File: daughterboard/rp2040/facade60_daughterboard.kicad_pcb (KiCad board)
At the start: 2 copper layers, 29.2 x 43.8 mm, 38 parts, among them J1 Conn_01x30, J2 USB_C_Receptacle_USB2.0, SW1 BOOT, SW2 RESET, U1 SRV05-4, U2 RT9013-33GB, U3 W25Q128JVS, U4 RP2040, Y1 12MHz

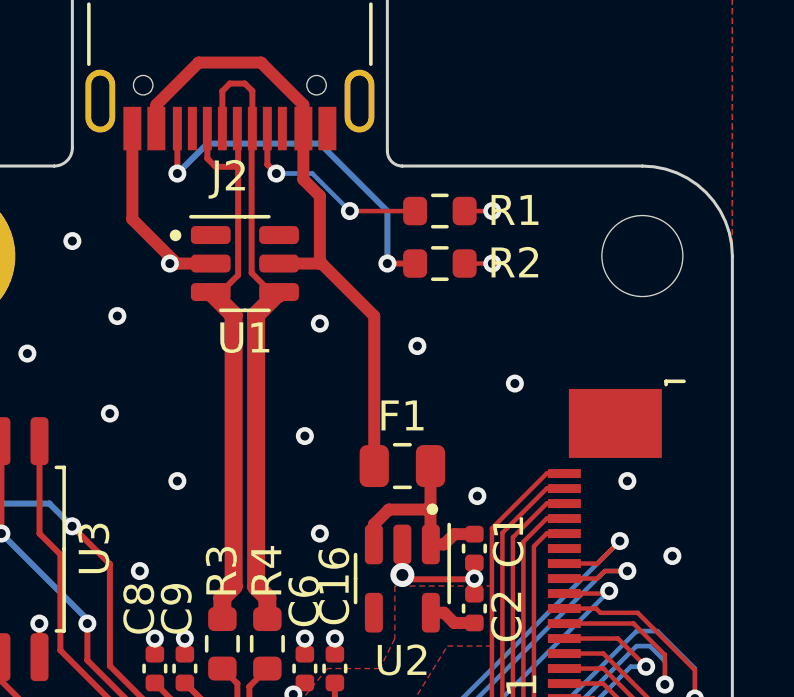
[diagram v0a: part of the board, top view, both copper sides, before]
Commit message: Replace R1 & R2 to 0402
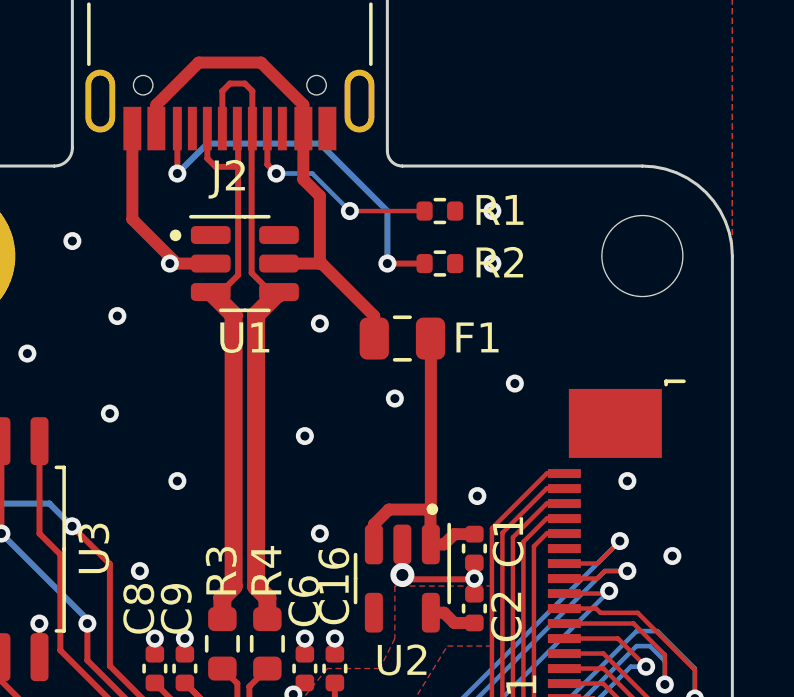
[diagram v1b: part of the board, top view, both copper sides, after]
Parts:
- R1, R2: footprint Resistor_SMD:R_0603_1608Metric -> Resistor_SMD:R_0402_1005Metric
- moved F1 4.25 mm to (125.5, 83.5)
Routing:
- net +5V: track 6.74 -> 11.2 mm
- net VBUS: track 21.0 -> 16.8 mm
- net GND: track 43.7 -> 41.9 mm
